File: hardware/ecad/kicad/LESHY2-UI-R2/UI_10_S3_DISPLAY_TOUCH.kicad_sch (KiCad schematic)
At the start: 34 parts, among them J1 Samtec FTSH-105-01-L-DV-K-P-TR, J2 GCT RFPC-SMA32-FN-175-A, J3 Hirose U.FL-R-SMT-1(80), SW1 Alps Alpine SKRTLAE010, SW2 Alps Alpine SKRTLAE010, U1 ESP32-S3-WROOM-1U-N16R8, U2 Texas Instruments TPD4E05U06D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, U3 KYOCERA AVX CP0603Q5425ENTR

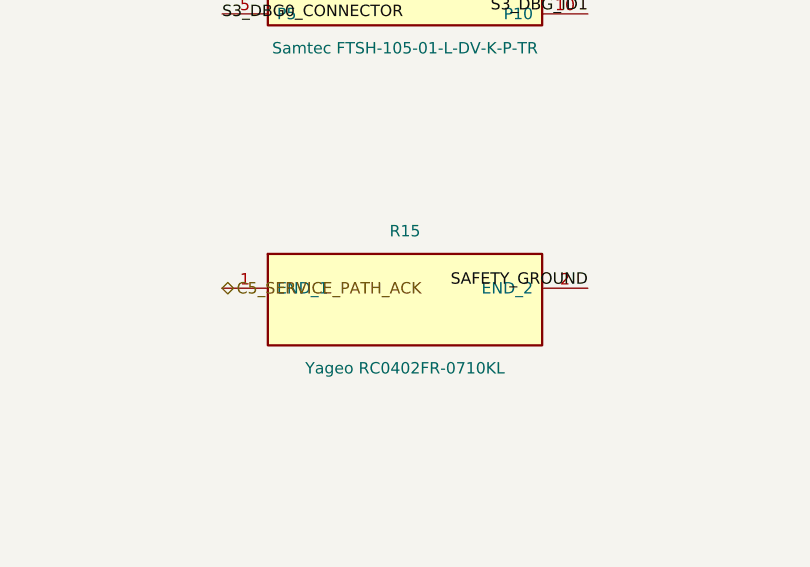
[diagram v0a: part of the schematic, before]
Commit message: Review R2 startup and fault-display sequencing
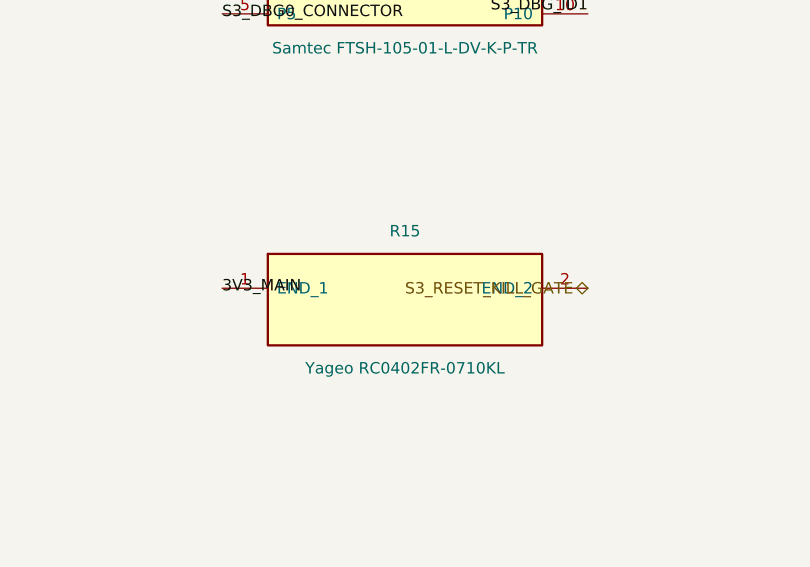
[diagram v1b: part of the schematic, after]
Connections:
- net C5_SERVICE_PATH_ACK is gone; now on net 3V3_MAIN: R15.1 (END_1)
- net SAFETY_GROUND: no longer R15.2 (END_2)
- new net S3_RESET_KILL_GATE: R15.2 (END_2)
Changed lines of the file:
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@@
 		)
 	)
-	(hierarchical_label "C5_SERVICE_PATH_ACK"
-		(shape bidirectional)
+	(label "3V3_MAIN"
 		(at 584.20 88.90 0)
 		(effects (font (size 1.27 1.27)))
 	)
-	(label "SAFETY_GROUND"
+	(hierarchical_label "S3_RESET_KILL_GATE"
+		(shape bidirectional)
 		(at 624.84 88.90 180)
 		(effects (font (size 1.27 1.27)) (justify right bottom))

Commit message: Mount display through direct UI-board ZIF
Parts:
- added J1: Hirose FH34SRJ-50S-0.5SH(50), Leshy2_R2:FH34SRJ-50S-0.5SH-50, symbol Leshy2_R2:hirose_fh34srj_50s_0_5sh_50
- renumbered J1 to J2, J2 to J3, J3 to J4
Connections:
- net 3V3_MAIN: now also J1.35 (PIN_35), J1.7 (PIN_7), J1.8 (PIN_8)
- net LCD_DB0: now also J1.32 (PIN_32)
- net LCD_DB1: now also J1.31 (PIN_31)
- net LCD_DB2: now also J1.30 (PIN_30)
- net LCD_DB3: now also J1.29 (PIN_29)
- net LCD_DB4: now also J1.28 (PIN_28)
- net LCD_DB5: now also J1.27 (PIN_27)
- net LCD_DB6: now also J1.26 (PIN_26)
- net LCD_DB7: now also J1.25 (PIN_25)
- net LCD_DC: now also J1.37 (PIN_37)
- net LCD_RST_N: now also J1.10 (PIN_10)
- net LCD_WR_N: now also J1.36 (PIN_36)
- net POWER_GROUND: now also J1.11 (PIN_11), J1.12 (PIN_12), J1.13 (PIN_13), J1.14 (PIN_14), J1.15 (PIN_15), J1.16 (PIN_16), J1.17 (PIN_17), J1.18 (PIN_18), J1.19 (PIN_19), J1.20 (PIN_20), J1.21 (PIN_21), J1.22 (PIN_22), J1.23 (PIN_23), J1.24 (PIN_24), J1.38 (PIN_38), J1.43 (PIN_43), J1.48 (PIN_48), J1.49 (PIN_49), J1.50 (PIN_50), J1.9 (PIN_9)
- net SYS_UI_I2C_SCL: now also J1.44 (PIN_44)
- net SYS_UI_I2C_SDA: now also J1.45 (PIN_45)
- net TOUCH_RST_N: now also J1.47 (PIN_47)
- new net LCD_LEDA_PROTECTED: J1.1 (PIN_1)
- new net LCD_LEDK: J1.2 (PIN_2), J1.3 (PIN_3)
- new net LCD_TOUCH_INT_RAW_N: J1.46 (PIN_46)
- new net LCD_VCI_3V3: J1.42 (PIN_42)
- new net LCD_VDDI_3V3: J1.40 (PIN_40), J1.41 (PIN_41)
- no-connect marks 13 -> 19
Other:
- title: Leshy2 R2 — S3 core, exact direct i8080-8 display, touch and S3 service -> Leshy2 R2 — S3 core, exact direct i8080-8 display through the UI-board ZIF, touch and S3 service
- moved on the sheet: J2, J3, J4, R1, R10, R11, R12, R13, R14, R15, R16, R17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

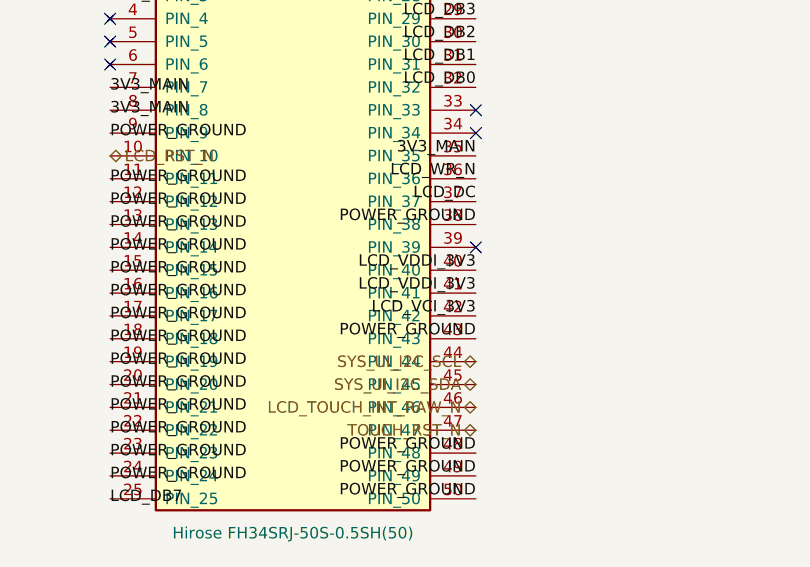
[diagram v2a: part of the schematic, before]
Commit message: Complete current R2 schematic and sourcing revalidation
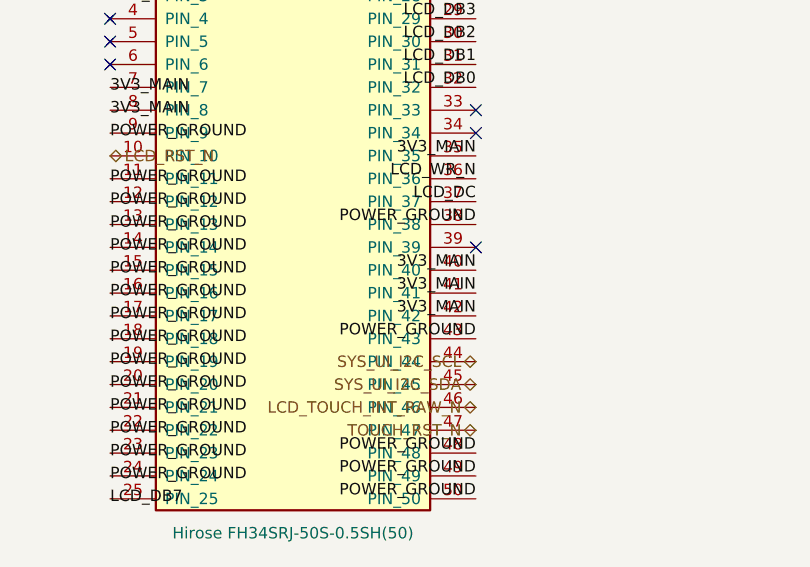
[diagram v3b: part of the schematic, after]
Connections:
- net LCD_VCI_3V3 is gone; now on net 3V3_MAIN: J1.42 (PIN_42)
- net LCD_VDDI_3V3 is gone; now on net 3V3_MAIN: J1.40 (PIN_40), J1.41 (PIN_41)
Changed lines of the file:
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@@
 	(no_connect (at 624.84 81.28)
 	)
-	(label "LCD_VDDI_3V3"
+	(label "3V3_MAIN"
 		(at 624.84 83.82 180)
 		(effects (font (size 1.27 1.27)) (justify right bottom))
 	)
-	(label "LCD_VDDI_3V3"
+	(label "3V3_MAIN"
 		(at 624.84 86.36 180)
 		(effects (font (size 1.27 1.27)) (justify right bottom))
 	)
-	(label "LCD_VCI_3V3"
+	(label "3V3_MAIN"
 		(at 624.84 88.90 180)
 		(effects (font (size 1.27 1.27)) (justify right bottom))

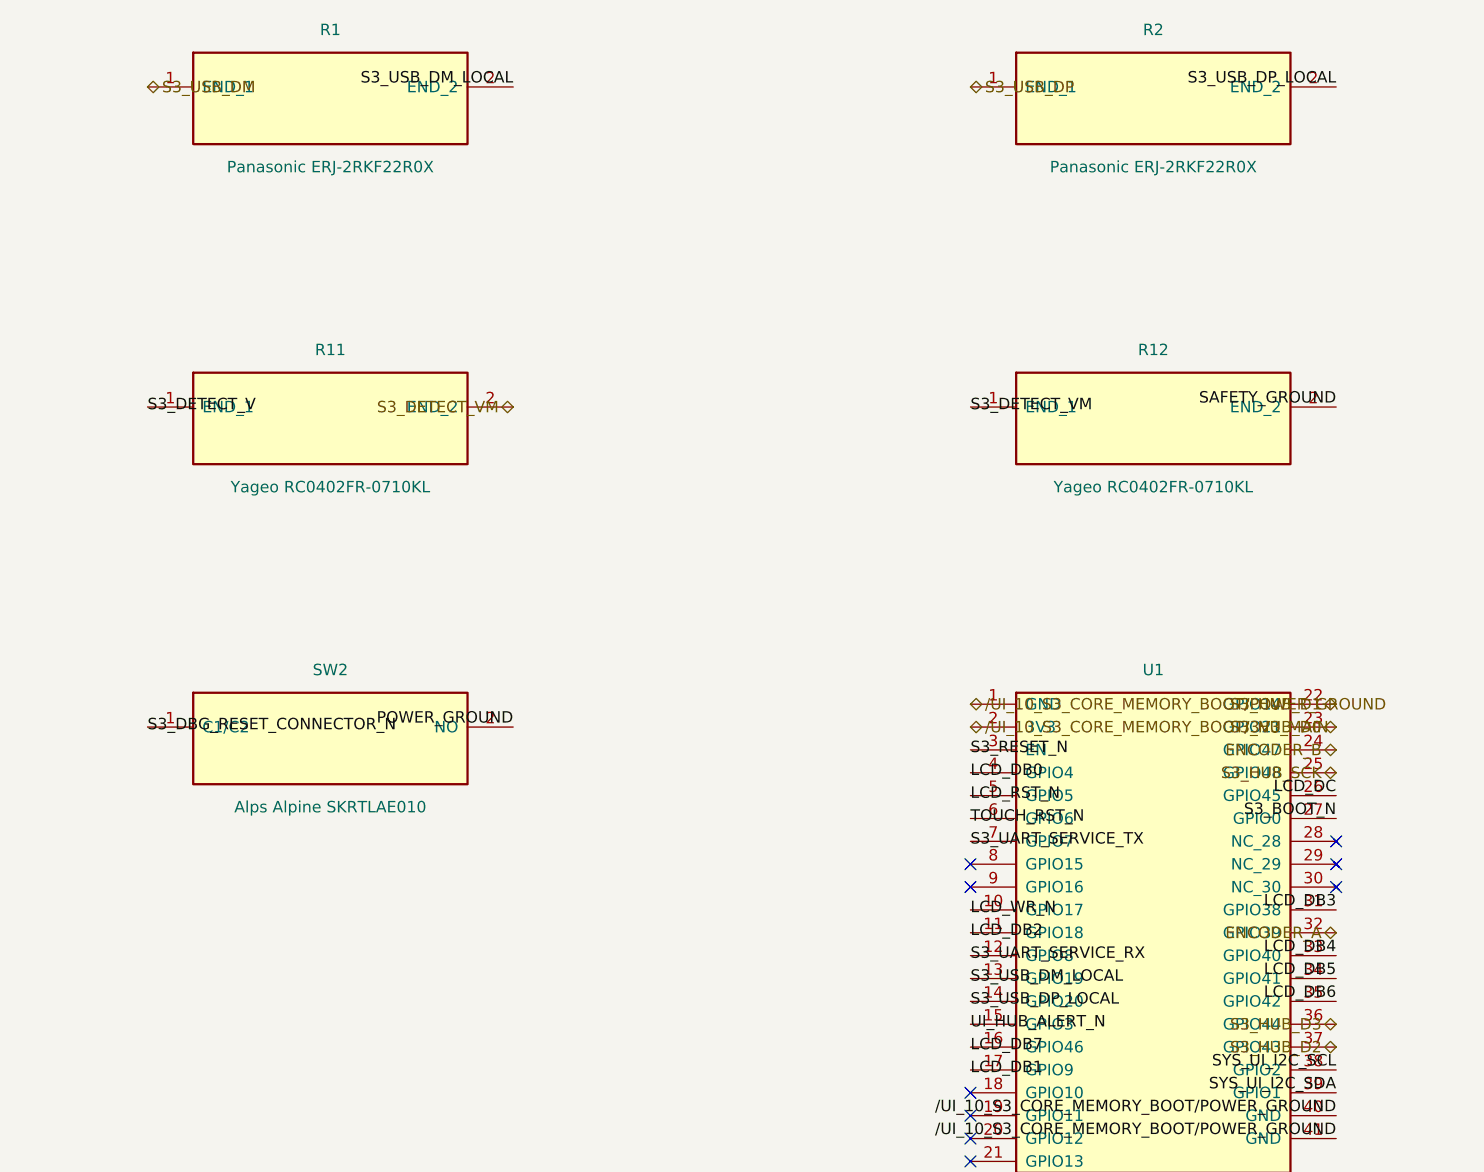
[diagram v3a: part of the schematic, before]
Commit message: Bind H6 RF and USB routing geometry
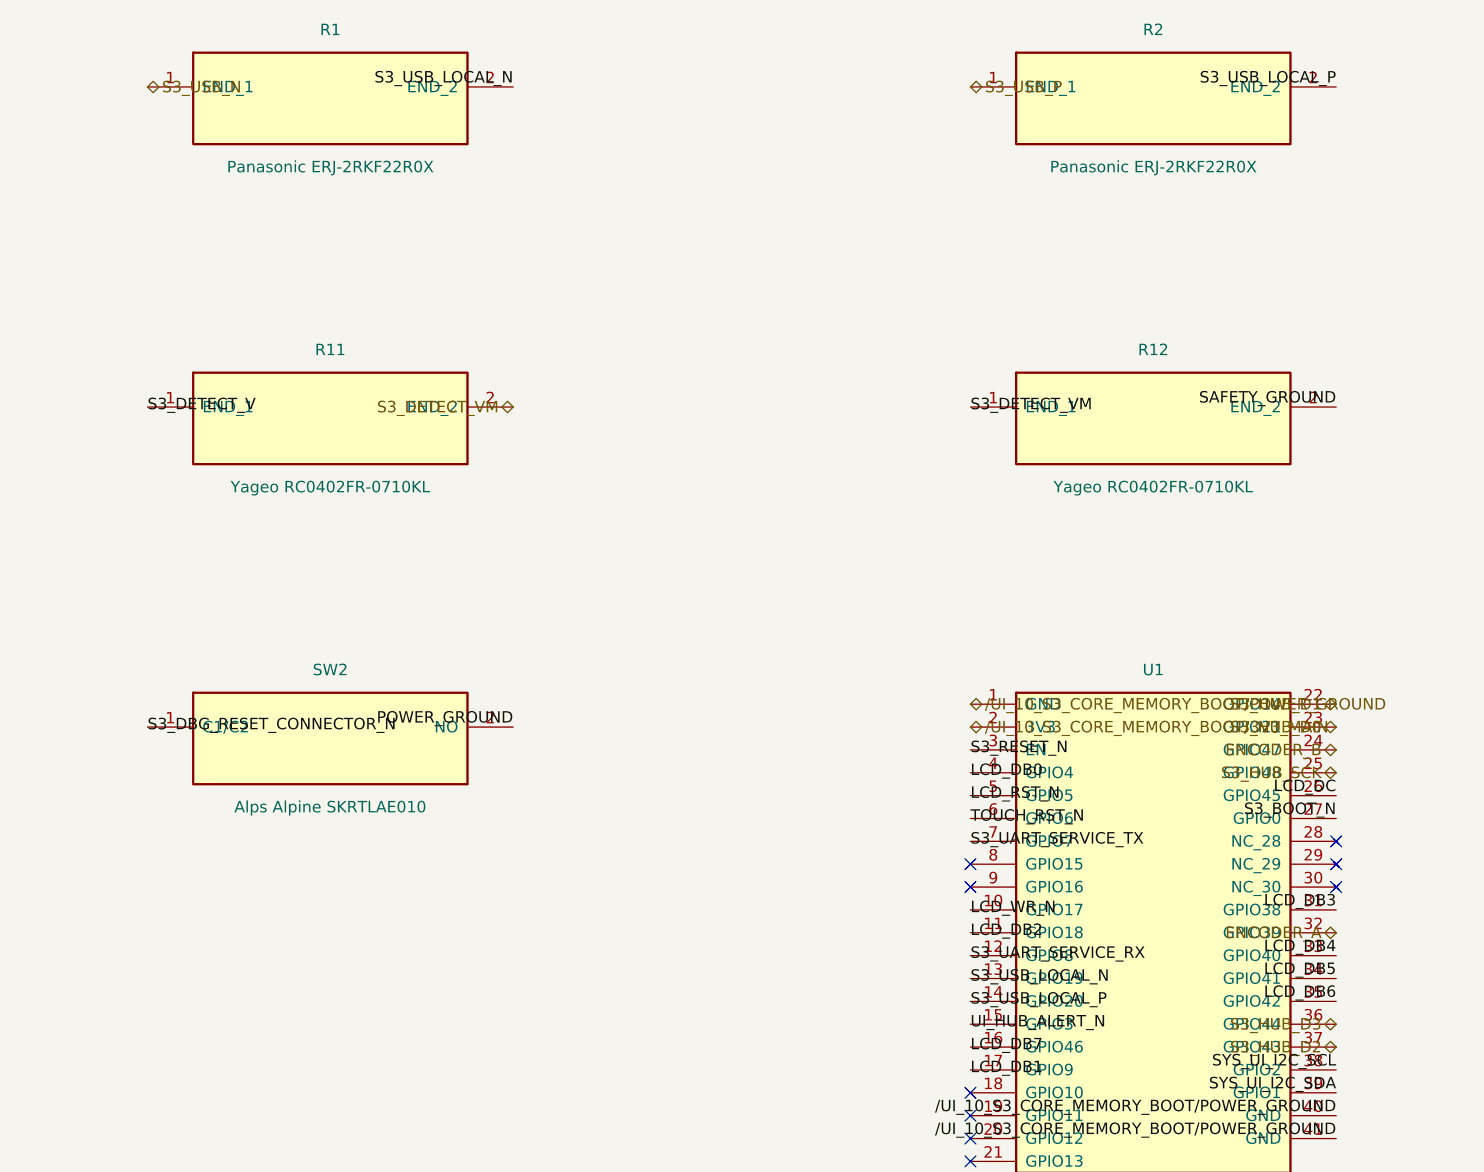
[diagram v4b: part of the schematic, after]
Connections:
- net S3_USB_DM renamed S3_USB_N
- net S3_USB_DM_LOCAL renamed S3_USB_LOCAL_N
- net S3_USB_DP renamed S3_USB_P
- net S3_USB_DP_LOCAL renamed S3_USB_LOCAL_P
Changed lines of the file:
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@@
 		)
 	)
-	(hierarchical_label "S3_USB_DM"
+	(hierarchical_label "S3_USB_N"
 		(shape bidirectional)
 		(at 949.96 50.80 0)
 		(effects (font (size 1.27 1.27)))
 	)
-	(label "S3_USB_DM_LOCAL"
+	(label "S3_USB_LOCAL_N"
 		(at 990.60 50.80 180)
 		(effects (font (size 1.27 1.27)) (justify right bottom))
@@
 		)
 	)
-	(hierarchical_label "S3_USB_DP"
+	(hierarchical_label "S3_USB_P"
 		(shape bidirectional)
 		(at 1041.40 50.80 0)
 		(effects (font (size 1.27 1.27)))
 	)
-	(label "S3_USB_DP_LOCAL"
+	(label "S3_USB_LOCAL_P"
 		(at 1082.04 50.80 180)
 		(effects (font (size 1.27 1.27)) (justify right bottom))
@@
 		(effects (font (size 1.27 1.27)))
 	)
-	(label "S3_USB_DM_LOCAL"
+	(label "S3_USB_LOCAL_N"
 		(at 1041.40 149.86 0)
 		(effects (font (size 1.27 1.27)))
 	)
-	(label "S3_USB_DP_LOCAL"
+	(label "S3_USB_LOCAL_P"
 		(at 1041.40 152.40 0)
 		(effects (font (size 1.27 1.27)))

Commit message: Canonicalize physical ground anchors
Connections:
- net /UI_10_S3_CORE_MEMORY_BOOT/POWER_GROUND is gone; now on net POWER_GROUND: U1.1 (GND), U1.40 (GND), U1.41 (GND)
- net S3_DBG_ESD_RETURN is gone; now on net POWER_GROUND: U2.3 (GND_3), U2.8 (GND_8)
- net S3_RF_GROUND is gone; now on net POWER_GROUND: J4.2 (SHELL), R17.2 (END_2)
- net S3_SMA_RF_GROUND is gone; now on net POWER_GROUND: J3.2 (GROUND_TOP_LEFT), J3.3 (GROUND_TOP_RIGHT), J3.4 (GROUND_BOTTOM_LEFT), J3.5 (GROUND_BOTTOM_RIGHT)
- net SAFETY_GROUND is gone; now on net POWER_GROUND: C1.2 (END_2), C3.2 (END_2), R12.2 (END_2), R14.2 (END_2)
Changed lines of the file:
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@@
 		(effects (font (size 1.27 1.27)))
 	)
-	(hierarchical_label "SAFETY_GROUND"
+	(hierarchical_label "POWER_GROUND"
 		(shape bidirectional)
 		(at 76.20 50.80 180)
@@
 		(effects (font (size 1.27 1.27)))
 	)
-	(label "SAFETY_GROUND"
+	(label "POWER_GROUND"
 		(at 259.08 50.80 180)
 		(effects (font (size 1.27 1.27)) (justify right bottom))
@@
 		(effects (font (size 1.27 1.27)))
 	)
-	(hierarchical_label "POWER_GROUND"
-		(shape bidirectional)
+	(label "POWER_GROUND"
 		(at 350.52 50.80 180)
 		(effects (font (size 1.27 1.27)) (justify right bottom))
@@
 		(effects (font (size 1.27 1.27)))
 	)
-	(label "S3_SMA_RF_GROUND"
+	(label "POWER_GROUND"
 		(at 767.08 52.07 0)
 		(effects (font (size 1.27 1.27)))
 	)
-	(label "S3_SMA_RF_GROUND"
+	(label "POWER_GROUND"
 		(at 767.08 54.61 0)
 		(effects (font (size 1.27 1.27)))
 	)
-	(label "S3_SMA_RF_GROUND"
+	(label "POWER_GROUND"
 		(at 807.72 49.53 180)
 		(effects (font (size 1.27 1.27)) (justify right bottom))
 	)
-	(label "S3_SMA_RF_GROUND"
+	(label "POWER_GROUND"
 		(at 807.72 52.07 180)
 		(effects (font (size 1.27 1.27)) (justify right bottom))
@@
 		(effects (font (size 1.27 1.27)))
 	)
-	(label "S3_RF_GROUND"
+	(label "POWER_GROUND"
 		(at 899.16 50.80 180)
 		(effects (font (size 1.27 1.27)) (justify right bottom))
@@
 		(effects (font (size 1.27 1.27)))
 	)
-	(label "SAFETY_GROUND"
+	(label "POWER_GROUND"
 		(at 1082.04 86.36 180)
 		(effects (font (size 1.27 1.27)) (justify right bottom))
@@
 		(effects (font (size 1.27 1.27)))
 	)
-	(label "SAFETY_GROUND"
+	(label "POWER_GROUND"
 		(at 76.20 121.92 180)
 		(effects (font (size 1.27 1.27)) (justify right bottom))
@@
 		(effects (font (size 1.27 1.27)))
 	)
-	(label "S3_RF_GROUND"
+	(label "POWER_GROUND"
 		(at 350.52 121.92 180)
 		(effects (font (size 1.27 1.27)) (justify right bottom))
@@
 		)
 	)
-	(hierarchical_label "/UI_10_S3_CORE_MEMORY_BOOT/POWER_GROUND"
-		(shape bidirectional)
+	(label "POWER_GROUND"
 		(at 1041.40 119.38 0)
 		(effects (font (size 1.27 1.27)))
@@
 		(effects (font (size 1.27 1.27)) (justify right bottom))
 	)
-	(label "/UI_10_S3_CORE_MEMORY_BOOT/POWER_GROUND"
+	(label "POWER_GROUND"
 		(at 1082.04 165.10 180)
 		(effects (font (size 1.27 1.27)) (justify right bottom))
 	)
-	(label "/UI_10_S3_CORE_MEMORY_BOOT/POWER_GROUND"
+	(label "POWER_GROUND"
 		(at 1082.04 167.64 180)
 		(effects (font (size 1.27 1.27)) (justify right bottom))
@@
 		(effects (font (size 1.27 1.27)))
 	)
-	(label "S3_DBG_ESD_RETURN"
+	(label "POWER_GROUND"
 		(at 675.64 127.00 0)
 		(effects (font (size 1.27 1.27)))
@@
 	(no_connect (at 716.28 124.46)
 	)
-	(label "S3_DBG_ESD_RETURN"
+	(label "POWER_GROUND"
 		(at 716.28 127.00 180)
 		(effects (font (size 1.27 1.27)) (justify right bottom))

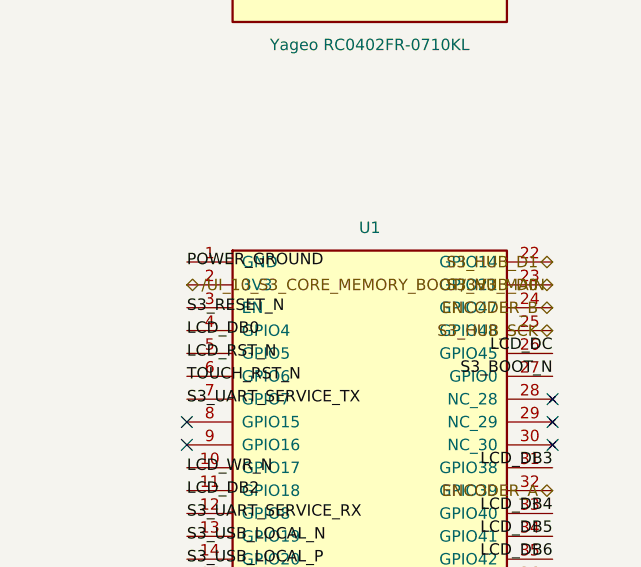
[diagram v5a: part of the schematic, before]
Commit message: Correct SMA geometry and module power; bind verification to current boards
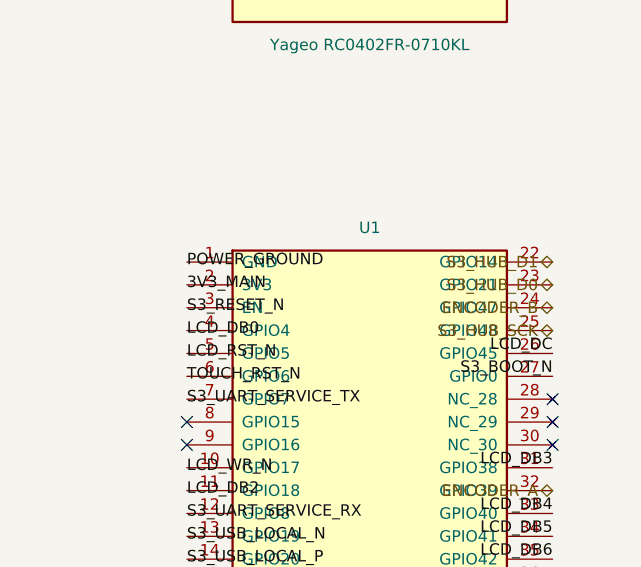
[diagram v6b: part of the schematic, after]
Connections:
- net /UI_10_S3_CORE_MEMORY_BOOT/3V3_MAIN is gone; now on net 3V3_MAIN: U1.2 (3V3)
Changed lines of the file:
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@@
 		(effects (font (size 1.27 1.27)))
 	)
-	(hierarchical_label "/UI_10_S3_CORE_MEMORY_BOOT/3V3_MAIN"
-		(shape bidirectional)
+	(label "3V3_MAIN"
 		(at 1041.40 121.92 0)
 		(effects (font (size 1.27 1.27)))
